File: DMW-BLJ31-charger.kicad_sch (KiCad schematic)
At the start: 24 parts, among them J1 BAT+, J10 gnd, J11 BAT+, J12 BAT-, J13 BAT+, J14 BAT-, J15 BAT+, J16 BAT-, J17 BAT-, J18 BAT+, J19 BAT-, J2 BAT-, J20 BAT+, J3 BAT+, J4 BAT+, J5 gnd, J6 gnd, J7 Vin, J8 Vin, J9 gnd

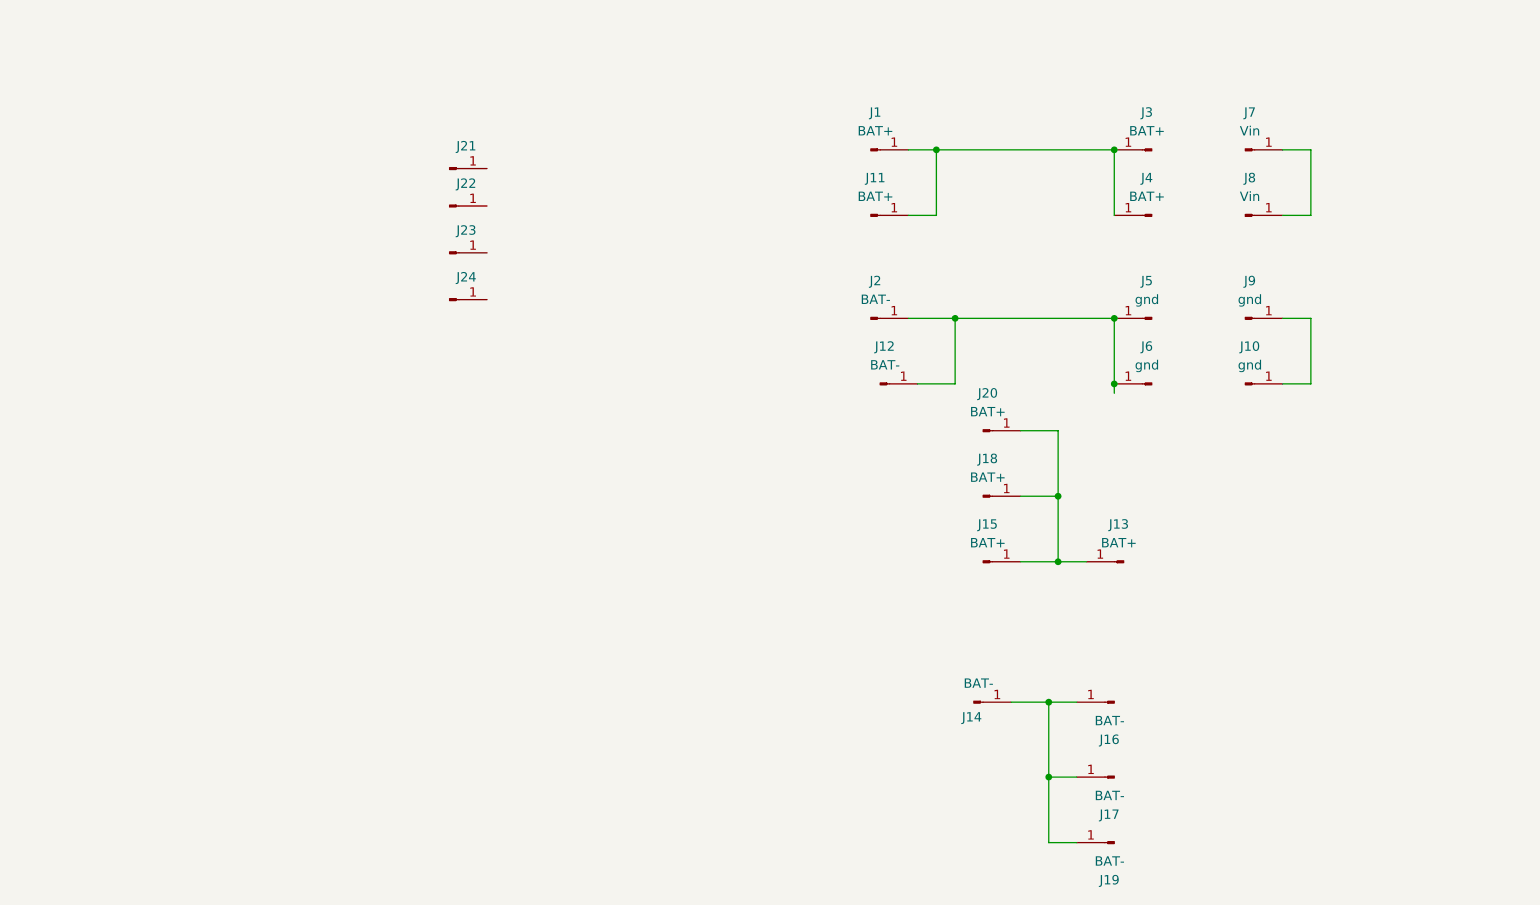
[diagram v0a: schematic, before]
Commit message: refined case pads
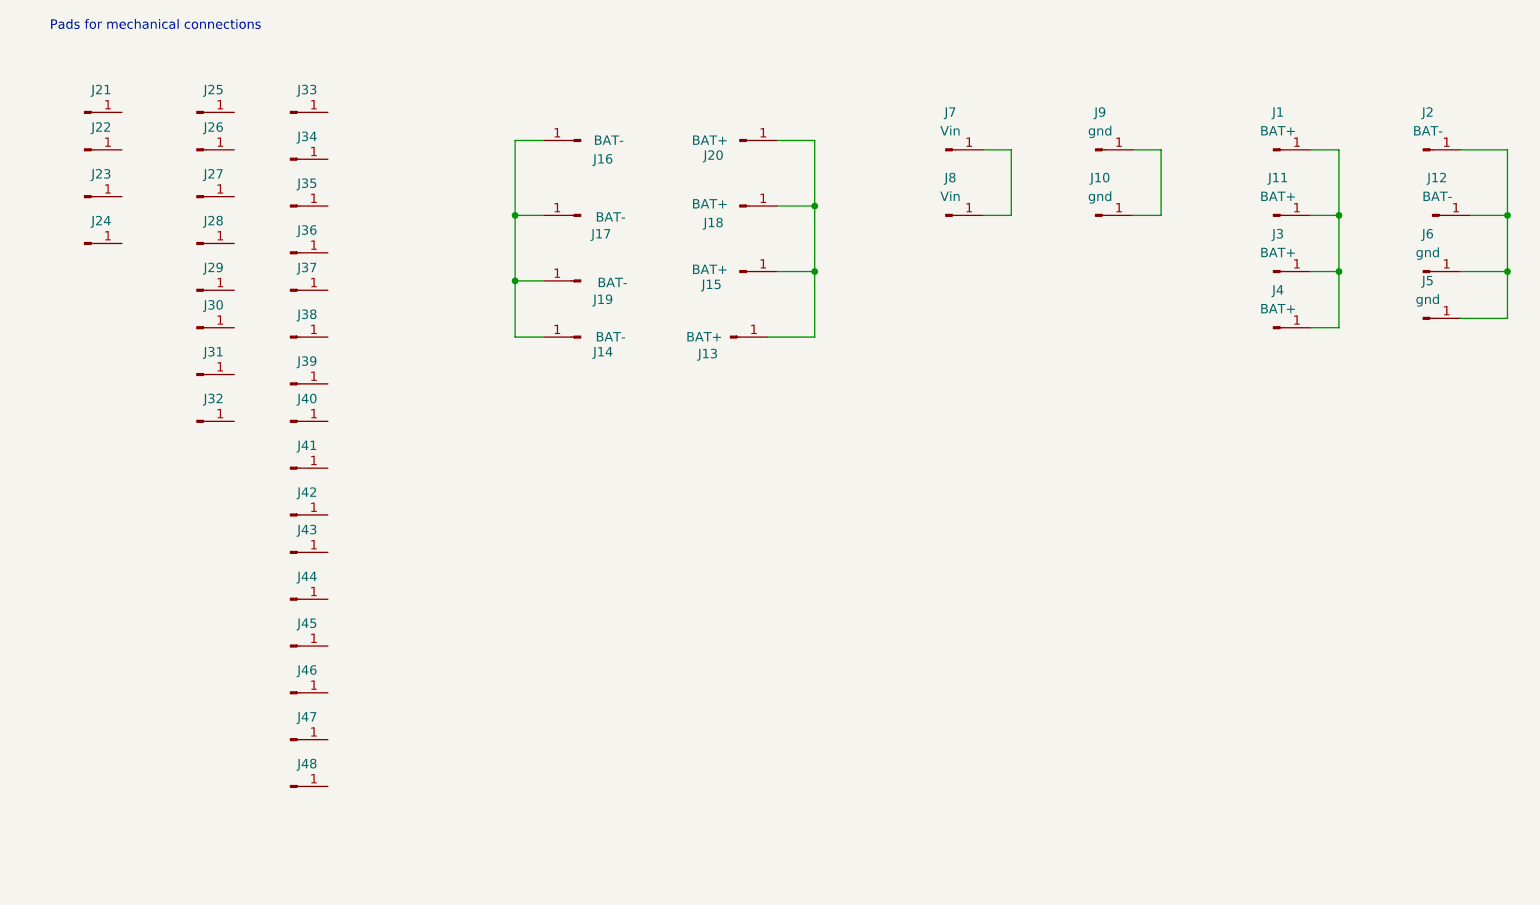
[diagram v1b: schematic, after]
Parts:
- added J25, J26, J27, J28, J29, J30, J31, J32, J33, J34, J35, J36, J37, J38, J39, J40, J41, J42, J43, J44, J45, J46, J47, J48: ~, Connector_Wire:SolderWire-0.25sqmm_1x01_D0.65mm_OD1.7mm, symbol Connector:Conn_01x01_Pin
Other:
- note added: "Pads for mechanical connections"
- moved on the sheet: J1, J10, J11, J12, J13, J14, J15, J16, J17, J18, J19, J2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

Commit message: move charger module to different side
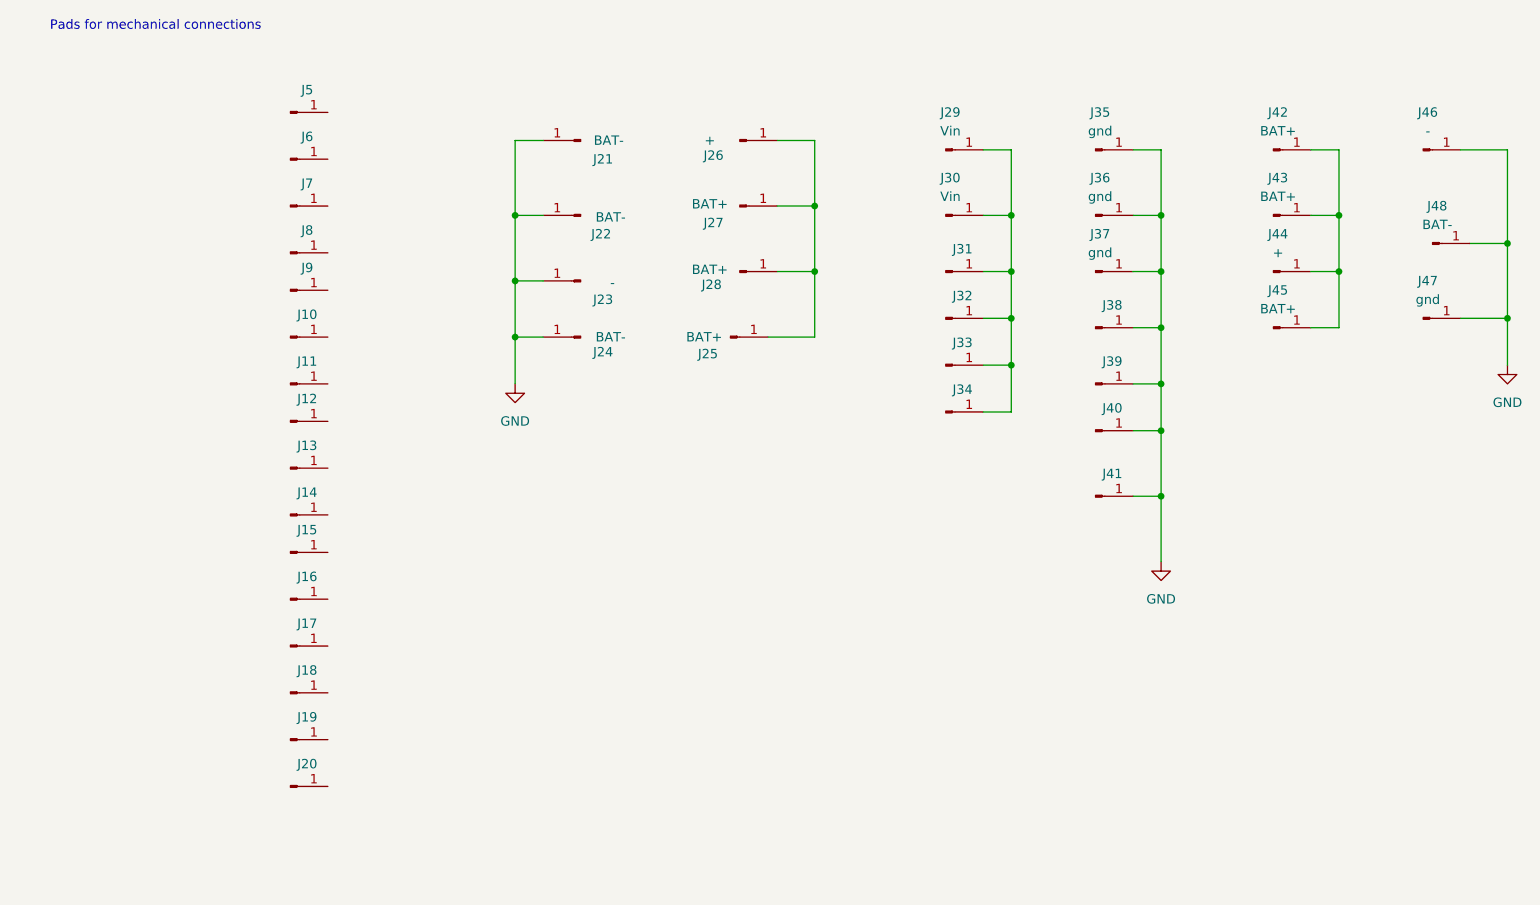
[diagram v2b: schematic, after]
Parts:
- removed J12: BAT-, Connector_Wire:SolderWire-0.25sqmm_1x01_D0.65mm_OD1.7mm, symbol Connector:Conn_01x01_Pin
- removed J29, J30, J31, J32: ~, Connector_Wire:SolderWire-0.25sqmm_1x01_D0.65mm_OD1.7mm, symbol Connector:Conn_01x01_Pin
- added J48: BAT-, Connector_Wire:SolderWire-0.25sqmm_1x01_D0.65mm_OD1.7mm, symbol Connector:Conn_01x01_Pin
- J23: renamed from J19; value BAT- -> -
- J26: renamed from J20; value BAT+ -> +
- J44: renamed from J3; value BAT+ -> +
- J46: renamed from J2; value BAT- -> -
- renumbered J38 to J10, J39 to J11, J40 to J12, J41 to J13, J42 to J14, J43 to J15, J44 to J16, J45 to J17, J46 to J18, J47 to J19, J48 to J20, J16 to J21, J17 to J22, J14 to J24, J13 to J25, J18 to J27, J15 to J28, J7 to J29, J8 to J30, J25 to J31, J28 to J32, J23 to J33, J24 to J34, J9 to J35, J10 to J36, J6 to J37, J21 to J38, J22 to J39, J26 to J40, J27 to J41, J1 to J42, J11 to J43, J4 to J45, J5 to J47, J33 to J5, J34 to J6, J35 to J7, J36 to J8, J37 to J9
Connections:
- net GND: now reaches J21.1 (Pin_1), J22.1 (Pin_1), J23.1 (Pin_1), J24.1 (Pin_1)
- net GND: now also J35.1 (Pin_1), J36.1 (Pin_1), J37.1 (Pin_1), J38.1 (Pin_1), J39.1 (Pin_1), J40.1 (Pin_1), J41.1 (Pin_1), J46.1 (Pin_1), J47.1 (Pin_1), J48.1 (Pin_1)
- net at J32.1 (Pin_1): now also J29.1 (Pin_1), J30.1 (Pin_1), J31.1 (Pin_1), J33.1 (Pin_1), J34.1 (Pin_1)
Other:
- moved on the sheet: J31, J32, J33, J34, J37, J38, J39, J40, J41
